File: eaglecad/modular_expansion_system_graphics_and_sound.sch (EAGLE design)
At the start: 44 parts, among them IC1 74LS244N, IC8 74LS244N, IC9-74HCU04 74LS04N, J1-WAIT-AND-INT WAIT-AND-INT, J1_ADDRESS_CON j1, J2_DATA_AND_POWER_CON j2, J3-VIDEO-OUT RCA, J4-AUDIO-LEFT RCA, J5-AUDIO-RIGHT RCA, Q2 2N2222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

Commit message: removed soft reset for vdp, added 12 voice sound
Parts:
- removed U$3: TRS80GS_DECODER, TMS99:TRS80GS_DECODER
- added C11, C12: 10uf, resistor:CPOL-USE2.5-6
- added C13, C14, C15: .1uf, resistor:C-US025-024X044
- added IC2: ATF22V10, TMS99:TRS80MXS_DECODER
- added IC3: 74LS74N, 74xx-us:74LS74N
- added J2-WAITS: WAITS, SparkFun-Connectors:CONN_04X2
- added U5, U6: SN76489, TMS99:SN76489
- C10, C2, C3, C4, C5, C6, C7, C8, C9: value (none) -> .1uf
- J1-INTERRUPTS: value WAIT-AND-INT -> INTERRUPTS
- renumbered J1-WAIT-AND-INT to J1-INTERRUPTS
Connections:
- removed net VID_RESET*: R9.1, U$3.RESET_OUT, U2.RESET*
- new net CLOCK_DIV_2: IC3A.Q, U5.CLOCK, U6.CLOCK
- new net CSR: IC2.CSR, U2.CSR*
- new net CSW: IC2.CSW, U2.CSW*
- new net N$10: C11.+, U5.SNDOUT
- new net N$11: IC2.SND4, U6.OE*, U6.WE*
- new net N$13: C12.+, U6.SNDOUT
- new net N$8: J2-WAITS.7, U5.READY
- new net N$9: IC2.SND3, U5.OE*, U5.WE*
- net A0: now also IC2.A0; no longer U$3.A0
- net A1: now also IC2.A1; no longer U$3.A1
- net A2: now also IC2.A2; no longer U$3.A2
- net A3: now also IC2.A3; no longer U$3.A3
- net A4: now also IC2.A4; no longer U$3.A4
- net A5: now also IC2.A5; no longer U$3.A5
- net A6: now also IC2.A6; no longer U$3.A6
- net A7: now also IC2.A7; no longer U$3.A7
- net D0: now also U5.D7, U6.D7
- net D1: now also U5.D6, U6.D6
- net D2: now also U5.D5, U6.D5
- net D3: now also U5.D4, U6.D4
- net D4: now also U5.D3, U6.D3
- net D5: now also U5.D2, U6.D2
- net D6: now also U5.D1, U6.D1
- net D7: now also U5.D0, U6.D0
- net GND: now also C13.2, C14.2, C15.2, IC2.GND, IC3B.CLK, IC3B.CLR, IC3B.D, IC3B.PRE, IC3P.GND, U5.GND, U6.GND; no longer U$3.GND
- net IN*: now also IC2.DEV_IN; no longer U$3.DEV_IN
- net JOY1_IN_ENABLE_N: now also IC2.JOY1; no longer U$3.JOY1
- net JOY1_IN_ENABLE_N1: now also IC2.JOY2; no longer U$3.JOY2
- net N$14: now also IC3A.!Q, IC3A.D; no longer U$3.CSW, U2.CSW*
- net N$15: now also J2-WAITS.2, U6.READY; no longer U$3.CSR, U2.CSR*
- net N$5: now also C12.-
- net N$64: now also C11.-
- net OUT*: now also IC2.DEV_OUT; no longer U$3.DEV_OUT
- net SN76489-CLOCK: now also IC3A.CLK
- net SND1_ENABLE_N: now also IC2.SND1; no longer U$3.SND1
- net SND1_READY: now also J2-WAITS.5; no longer J1-INTERRUPTS.6
- net SND2_ENABLE_N: now also IC2.SND2; no longer U$3.SND2
- net SND2_READY: now also J2-WAITS.3; no longer J1-INTERRUPTS.4
- net SYSRES*: now also R9.1, U2.RESET*; no longer U$3.RESET_IN
- net VCC: now also C13.1, C14.1, C15.1, IC2.VCC, IC3A.CLR, IC3A.PRE, IC3P.VCC, U5.VCC, U6.VCC; no longer U$3.VCC
- net VDP_MODE: now also IC2.MODE; no longer U$3.MODE
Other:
- moved on the sheet: R9

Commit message: updated readme
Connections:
- removed net CLOCK_DIV_2: IC3A.Q, U5.CLOCK, U6.CLOCK
- new net CLOCK_DIV_4: IC3B.Q, U5.CLOCK, U6.CLOCK
- new net N$6: IC3A.Q, IC3B.CLK
- new net N$7: IC3B.!Q, IC3B.D
- net GND: no longer IC3B.CLK, IC3B.CLR, IC3B.D, IC3B.PRE
- net VCC: now also IC3B.CLR, IC3B.PRE
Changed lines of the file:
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@@
 <part name="P+14" library="supply1" library_urn="urn:adsk.eagle:library:371" deviceset="VCC" device=""/>
 <part name="C15" library="resistor" library_urn="urn:adsk.eagle:library:348" deviceset="C-US" device="025-024X044" package3d_urn="urn:adsk.eagle:package:23630/1" value=".1uf"/>
-<part name="GND14" library="supply1" library_urn="urn:adsk.eagle:library:371" deviceset="GND" device=""/>
+<part name="P+15" library="supply1" library_urn="urn:adsk.eagle:library:371" deviceset="VCC" device=""/>
 </parts>
 <sheets>
@@
 <attribute name="VALUE" x="355.6" y="257.81" size="1.778" layer="96"/>
 </instance>
-<instance part="GND14" gate="1" x="350.52" y="256.54" smashed="yes">
-<attribute name="VALUE" x="347.98" y="254" size="1.778" layer="96"/>
+<instance part="P+15" gate="VCC" x="347.98" y="275.59" smashed="yes">
+<attribute name="VALUE" x="345.44" y="273.05" size="1.778" layer="96" rot="R90"/>
 </instance>
 </instances>
@@
 <wire x1="408.94" y1="261.62" x2="408.94" y2="259.08" width="0.1524" layer="91"/>
 </segment>
-<segment>
-<pinref part="GND14" gate="1" pin="GND"/>
-<pinref part="IC3" gate="B" pin="CLR"/>
-<wire x1="350.52" y1="259.08" x2="350.52" y2="262.89" width="0.1524" layer="91"/>
-<pinref part="IC3" gate="B" pin="CLK"/>
-<wire x1="350.52" y1="262.89" x2="350.52" y2="265.43" width="0.1524" layer="91"/>
-<junction x="350.52" y="262.89"/>
-<pinref part="IC3" gate="B" pin="D"/>
-<wire x1="350.52" y1="265.43" x2="350.52" y2="270.51" width="0.1524" layer="91"/>
-<junction x="350.52" y="265.43"/>
-<pinref part="IC3" gate="B" pin="PRE"/>
-<wire x1="350.52" y1="270.51" x2="350.52" y2="273.05" width="0.1524" layer="91"/>
-<junction x="350.52" y="270.51"/>
-</segment>
 </net>
 <net name="VCC" class="0">
@@
 <junction x="350.52" y="295.91"/>
 </segment>
+<segment>
+<pinref part="IC3" gate="B" pin="PRE"/>
+<wire x1="350.52" y1="273.05" x2="347.98" y2="273.05" width="0.1524" layer="91"/>
+<wire x1="347.98" y1="273.05" x2="347.98" y2="262.89" width="0.1524" layer="91"/>
+<pinref part="IC3" gate="B" pin="CLR"/>
+<wire x1="347.98" y1="262.89" x2="350.52" y2="262.89" width="0.1524" layer="91"/>
+<pinref part="P+15" gate="VCC" pin="VCC"/>
+<junction x="347.98" y="273.05"/>
+</segment>
 </net>
 <net name="COMVID-OUT" class="0">
@@
 </segment>
 </net>
-<net name="CLOCK_DIV_2" class="0">
-<segment>
-<pinref part="IC3" gate="A" pin="Q"/>
-<wire x1="375.92" y1="295.91" x2="375.92" y2="313.69" width="0.1524" layer="91"/>
-<wire x1="375.92" y1="313.69" x2="322.58" y2="313.69" width="0.1524" layer="91"/>
+<net name="CLOCK_DIV_4" class="0">
+<segment>
 <wire x1="322.58" y1="313.69" x2="322.58" y2="287.02" width="0.1524" layer="91"/>
 <pinref part="U5" gate="G$1" pin="CLOCK"/>
@@
 <wire x1="436.88" y1="287.02" x2="450.85" y2="287.02" width="0.1524" layer="91"/>
 <wire x1="450.85" y1="287.02" x2="450.85" y2="313.69" width="0.1524" layer="91"/>
-<wire x1="450.85" y1="313.69" x2="375.92" y2="313.69" width="0.1524" layer="91"/>
-<junction x="375.92" y="313.69"/>
+<wire x1="450.85" y1="313.69" x2="383.54" y2="313.69" width="0.1524" layer="91"/>
+<pinref part="IC3" gate="B" pin="Q"/>
+<wire x1="383.54" y1="313.69" x2="322.58" y2="313.69" width="0.1524" layer="91"/>
+<wire x1="375.92" y1="273.05" x2="383.54" y2="273.05" width="0.1524" layer="91"/>
+<wire x1="383.54" y1="273.05" x2="383.54" y2="313.69" width="0.1524" layer="91"/>
+<junction x="383.54" y="313.69"/>
 </segment>
 </net>
@@
 </segment>
 </net>
+<net name="N$6" class="0">
+<segment>
+<pinref part="IC3" gate="A" pin="Q"/>
+<wire x1="375.92" y1="295.91" x2="378.46" y2="295.91" width="0.1524" layer="91"/>
+<wire x1="378.46" y1="295.91" x2="378.46" y2="276.86" width="0.1524" layer="91"/>
+<wire x1="378.46" y1="276.86" x2="345.44" y2="276.86" width="0.1524" layer="91"/>
+<wire x1="345.44" y1="276.86" x2="345.44" y2="265.43" width="0.1524" layer="91"/>
+<pinref part="IC3" gate="B" pin="CLK"/>
+<wire x1="345.44" y1="265.43" x2="350.52" y2="265.43" width="0.1524" layer="91"/>
+</segment>
+</net>
+<net name="N$7" class="0">
+<segment>
+<pinref part="IC3" gate="B" pin="!Q"/>
+<wire x1="375.92" y1="262.89" x2="375.92" y2="256.54" width="0.1524" layer="91"/>
+<wire x1="375.92" y1="256.54" x2="344.17" y2="256.54" width="0.1524" layer="91"/>
+<wire x1="344.17" y1="256.54" x2="344.17" y2="270.51" width="0.1524" layer="91"/>
+<pinref part="IC3" gate="B" pin="D"/>
+<wire x1="344.17" y1="270.51" x2="350.52" y2="270.51" width="0.1524" layer="91"/>
+</segment>
+</net>

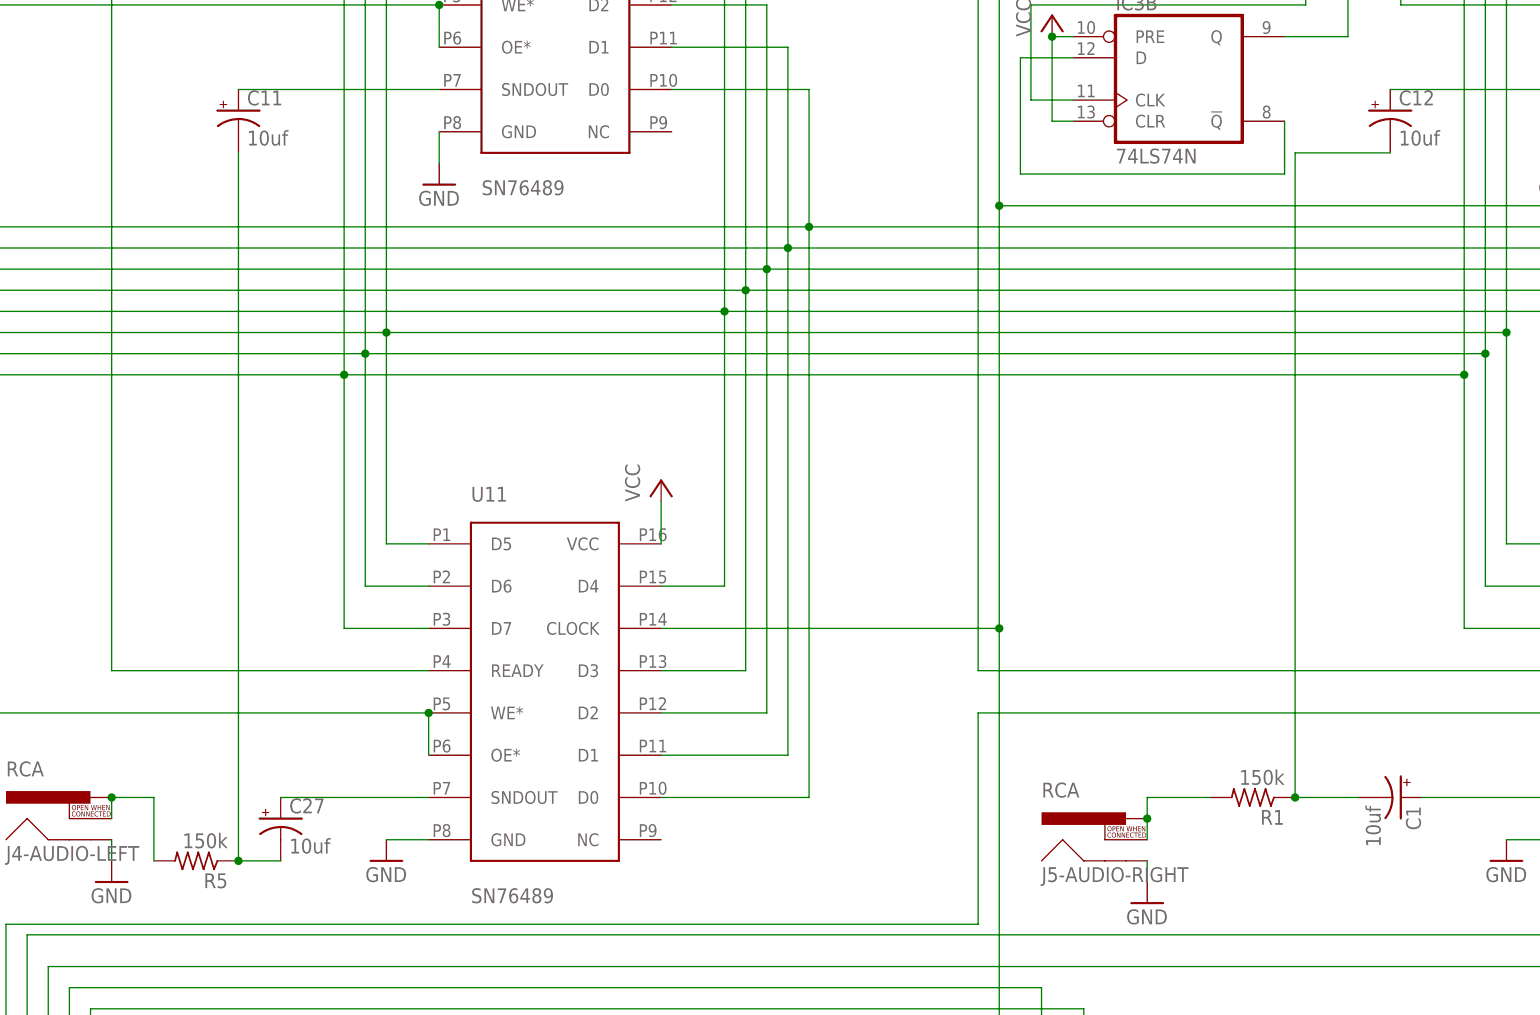
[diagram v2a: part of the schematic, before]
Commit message: tweaked sound circuit
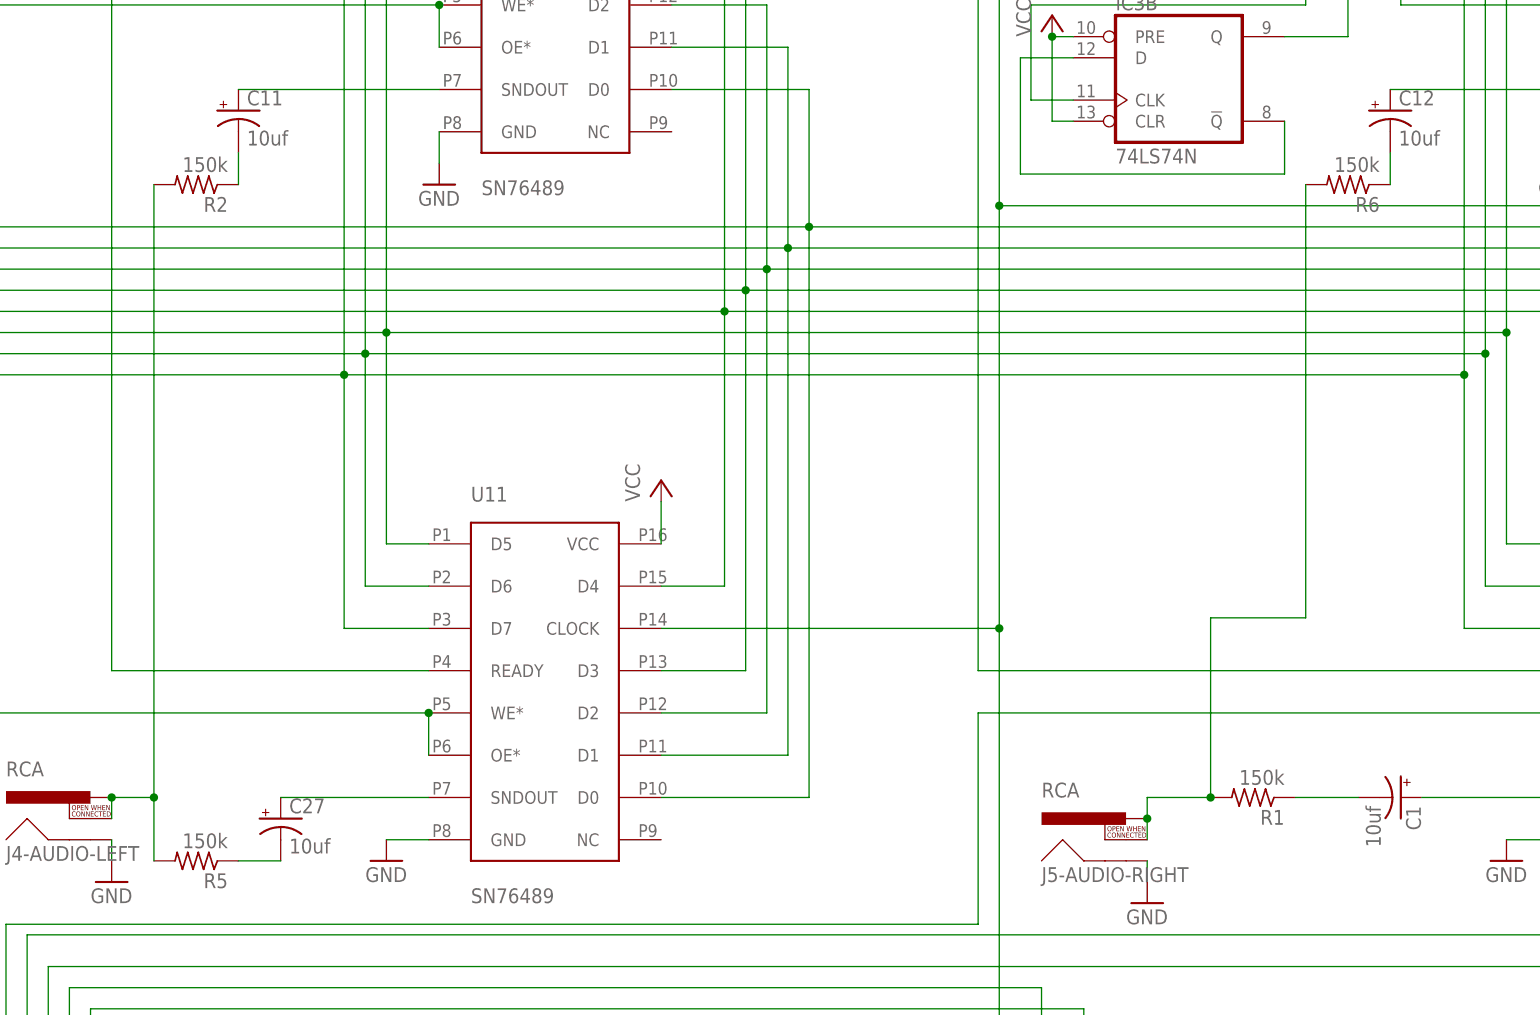
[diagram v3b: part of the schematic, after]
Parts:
- added R2, R6: 150k, resistor:R-US_0207/2V
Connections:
- new net N$16: C1.-, R1.1
- new net N$17: C11.-, R2.1
- net N$1: now also R2.2
- net N$24: now also R6.2
- net N$5: now also R6.1; no longer C1.-, R1.1
- net N$64: no longer C11.-
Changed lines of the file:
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@@
 <part name="C15" library="resistor" library_urn="urn:adsk.eagle:library:348" deviceset="C-US" device="025-024X044" package3d_urn="urn:adsk.eagle:package:23630/1" value=".1uf"/>
 <part name="P+15" library="supply1" library_urn="urn:adsk.eagle:library:371" deviceset="VCC" device=""/>
+<part name="R2" library="resistor" library_urn="urn:adsk.eagle:library:348" deviceset="R-US_" device="0207/2V" package3d_urn="urn:adsk.eagle:package:23490/1" value="150k"/>
+<part name="R6" library="resistor" library_urn="urn:adsk.eagle:library:348" deviceset="R-US_" device="0207/2V" package3d_urn="urn:adsk.eagle:package:23490/1" value="150k"/>
 </parts>
 <sheets>
@@
 <instance part="P+15" gate="VCC" x="347.98" y="275.59" smashed="yes">
 <attribute name="VALUE" x="345.44" y="273.05" size="1.778" layer="96" rot="R90"/>
+</instance>
+<instance part="R2" gate="G$1" x="245.11" y="255.27" smashed="yes" rot="R180">
+<attribute name="NAME" x="248.92" y="253.7714" size="1.778" layer="95" rot="R180"/>
+<attribute name="VALUE" x="248.92" y="258.572" size="1.778" layer="96" rot="R180"/>
+</instance>
+<instance part="R6" gate="G$1" x="383.54" y="255.27" smashed="yes" rot="R180">
+<attribute name="NAME" x="387.35" y="253.7714" size="1.778" layer="95" rot="R180"/>
+<attribute name="VALUE" x="387.35" y="258.572" size="1.778" layer="96" rot="R180"/>
 </instance>
 </instances>
@@
 <pinref part="C27" gate="G$1" pin="-"/>
 <pinref part="R5" gate="G$1" pin="1"/>
-<wire x1="250.19" y1="173.99" x2="250.19" y2="259.08" width="0.1524" layer="91"/>
-<junction x="250.19" y="173.99"/>
-<pinref part="C11" gate="G$1" pin="-"/>
 </segment>
 </net>
@@
 <wire x1="359.41" y1="181.61" x2="359.41" y2="179.07" width="0.1524" layer="91"/>
 <junction x="359.41" y="179.07"/>
+<pinref part="R6" gate="G$1" pin="2"/>
+<wire x1="378.46" y1="255.27" x2="378.46" y2="203.2" width="0.1524" layer="91"/>
+<wire x1="378.46" y1="203.2" x2="367.03" y2="203.2" width="0.1524" layer="91"/>
+<wire x1="367.03" y1="203.2" x2="367.03" y2="181.61" width="0.1524" layer="91"/>
+<junction x="367.03" y="181.61"/>
 </segment>
 </net>
@@
 <wire x1="240.03" y1="181.61" x2="240.03" y2="173.99" width="0.1524" layer="91"/>
 <junction x="234.95" y="181.61"/>
+<pinref part="R2" gate="G$1" pin="2"/>
+<wire x1="240.03" y1="255.27" x2="240.03" y2="181.61" width="0.1524" layer="91"/>
+<junction x="240.03" y="181.61"/>
 </segment>
 </net>
@@
 </segment>
 </net>
-<net name="N$5" class="0">
-<segment>
-<pinref part="C1" gate="G$1" pin="-"/>
-<pinref part="R1" gate="G$1" pin="1"/>
-<wire x1="384.81" y1="181.61" x2="377.19" y2="181.61" width="0.1524" layer="91"/>
-<wire x1="377.19" y1="181.61" x2="377.19" y2="259.08" width="0.1524" layer="91"/>
-<junction x="377.19" y="181.61"/>
-<pinref part="C12" gate="G$1" pin="-"/>
-<wire x1="377.19" y1="259.08" x2="388.62" y2="259.08" width="0.1524" layer="91"/>
-</segment>
-</net>
 <net name="WR*" class="0">
 <segment>
@@
 </segment>
 </net>
+<net name="N$16" class="0">
+<segment>
+<pinref part="R1" gate="G$1" pin="1"/>
+<pinref part="C1" gate="G$1" pin="-"/>
+<wire x1="384.81" y1="181.61" x2="377.19" y2="181.61" width="0.1524" layer="91"/>
+</segment>
+</net>
+<net name="N$5" class="0">
+<segment>
+<pinref part="C12" gate="G$1" pin="-"/>
+<pinref part="R6" gate="G$1" pin="1"/>
+<wire x1="388.62" y1="259.08" x2="388.62" y2="255.27" width="0.1524" layer="91"/>
+</segment>
+</net>
+<net name="N$17" class="0">
+<segment>
+<pinref part="C11" gate="G$1" pin="-"/>
+<pinref part="R2" gate="G$1" pin="1"/>
+<wire x1="250.19" y1="259.08" x2="250.19" y2="255.27" width="0.1524" layer="91"/>
+</segment>
+</net>
